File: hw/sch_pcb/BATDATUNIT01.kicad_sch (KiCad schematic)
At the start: 109 parts, among them IC1 MAX14502AETL+, J1 USBC_USB4105-GF-A, J22 HEADER_2x03, J4 46436-9327, J9 SD_Card-FPS009-4200-0, Q1 BC817-25, Q2 BC817-25, Q3 BC817-25, Q4 BC817-25, SW3 KMT031, SW3 SKRTLAE010, SW4 KMT031, SW4 SKRTLAE010, U10 ATMEGA1284P-AU, U10 TCA4307, U11 PCF85263A, U12 TMUX1574DYYR, U2 USBLC6-2SC6, U3 FT260Q-T, U4 PCA9541ABS/01, U6 AT24CS64-SSHM, U6 SHT35-DIS, Y1 8 MHz, Y2 ABS07-120-32.768KHZ-T

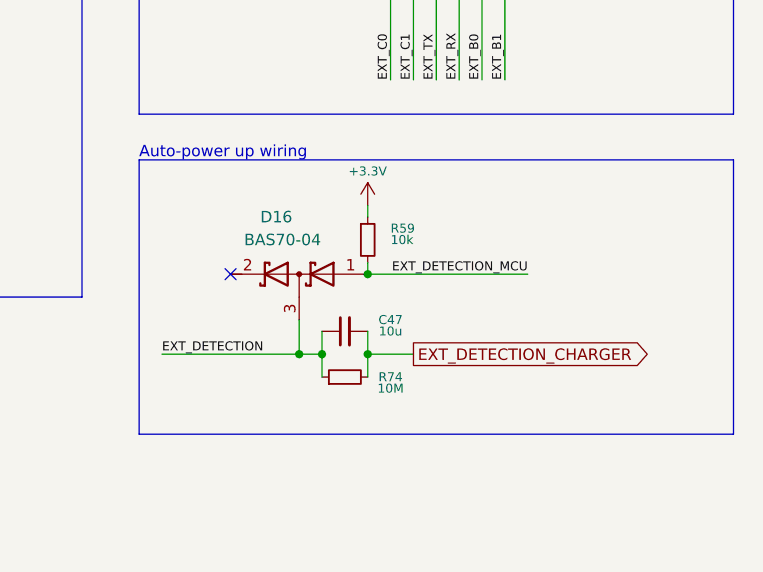
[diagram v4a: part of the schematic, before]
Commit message: Layout update, place and route new added components
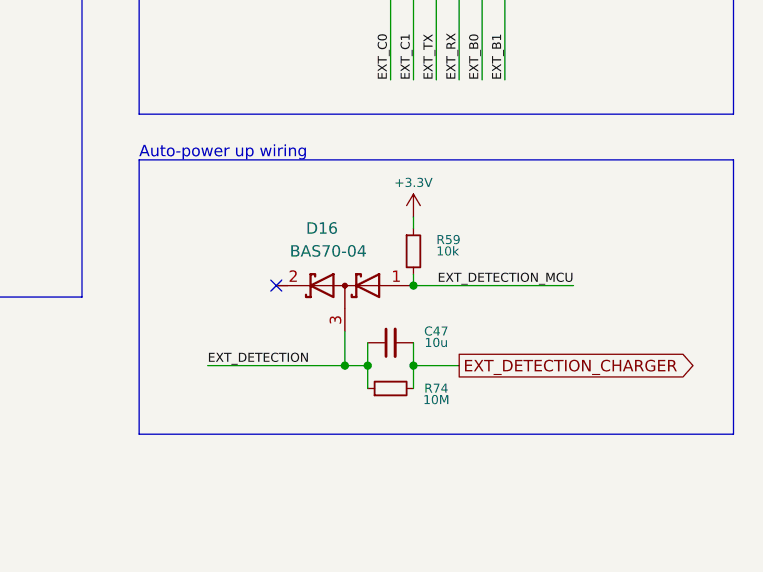
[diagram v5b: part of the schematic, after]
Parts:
- C47: footprint (none) -> Capacitor_SMD:C_0805_2012Metric
- R74: footprint (none) -> Resistor_SMD:R_0805_2012Metric
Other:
- moved on the sheet: C47, D16, R59, R74
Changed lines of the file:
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@@
   (junction (at 80.01 209.55) (diameter 0) (color 0 0 0 0)
   )
-  (junction (at 358.14 241.3) (diameter 0) (color 0 0 0 0)
+  (junction (at 363.22 242.57) (diameter 0) (color 0 0 0 0)
   )
   (junction (at 142.24 248.92) (diameter 0) (color 0 0 0 0)
@@
   (junction (at 40.64 262.89) (diameter 1.016) (color 0 0 0 0)
   )
-  (junction (at 363.22 241.3) (diameter 0) (color 0 0 0 0)
+  (junction (at 368.3 242.57) (diameter 0) (color 0 0 0 0)
   )
   (junction (at 156.21 144.78) (diameter 0) (color 0 0 0 0)
@@
   (junction (at 162.56 35.56) (diameter 0) (color 0 0 0 0)
   )
-  (junction (at 355.6 241.3) (diameter 0) (color 0 0 0 0)
+  (junction (at 360.68 242.57) (diameter 0) (color 0 0 0 0)
   )
   (junction (at 53.34 43.18) (diameter 0) (color 0 0 0 0)
@@
   (junction (at 36.83 262.89) (diameter 1.016) (color 0 0 0 0)
   )
-  (junction (at 363.22 232.41) (diameter 0) (color 0 0 0 0)
+  (junction (at 368.3 233.68) (diameter 0) (color 0 0 0 0)
   )
   (junction (at 275.59 220.98) (diameter 1.016) (color 0 0 0 0)
@@
   (no_connect (at 388.62 173.99))
   (no_connect (at 184.15 182.88))
-  (no_connect (at 347.98 232.41))
+  (no_connect (at 353.06 233.68))
   (no_connect (at 388.62 176.53))
   (no_connect (at 92.71 124.46))
@@
     (stroke (width 0) (type default))
   )
-  (wire (pts (xy 363.22 241.3) (xy 363.22 243.84))
+  (wire (pts (xy 368.3 242.57) (xy 368.3 245.11))
     (stroke (width 0) (type default))
   )
@@
     (stroke (width 0) (type default))
   )
-  (wire (pts (xy 340.36 241.3) (xy 355.6 241.3))
+  (wire (pts (xy 345.44 242.57) (xy 360.68 242.57))
     (stroke (width 0) (type default))
   )
@@
     (stroke (width 0) (type default))
   )
-  (wire (pts (xy 355.6 241.3) (xy 358.14 241.3))
+  (wire (pts (xy 360.68 242.57) (xy 363.22 242.57))
     (stroke (width 0) (type default))
   )
@@
     (stroke (width 0) (type default))
   )
-  (wire (pts (xy 363.22 241.3) (xy 368.3 241.3))
+  (wire (pts (xy 368.3 242.57) (xy 373.38 242.57))
     (stroke (width 0) (type default))
   )
@@
     (stroke (width 0) (type default))
   )
-  (wire (pts (xy 363.22 224.79) (xy 363.22 226.06))
+  (wire (pts (xy 368.3 226.06) (xy 368.3 227.33))
     (stroke (width 0) (type default))
   )
@@
     (stroke (width 0) (type default))
   )
-  (wire (pts (xy 363.22 232.41) (xy 381 232.41))
+  (wire (pts (xy 368.3 233.68) (xy 386.08 233.68))
     (stroke (width 0) (type default))
   )
@@
     (stroke (width 0) (type default))
   )
-  (wire (pts (xy 363.22 231.14) (xy 363.22 232.41))
+  (wire (pts (xy 368.3 232.41) (xy 368.3 233.68))
     (stroke (width 0) (type default))
   )
@@
     (stroke (width 0) (type default))
   )
-  (wire (pts (xy 358.14 238.76) (xy 358.14 241.3))
+  (wire (pts (xy 363.22 240.03) (xy 363.22 242.57))
     (stroke (width 0) (type default))
   )
@@
     (stroke (width 0) (type default))
   )
-  (wire (pts (xy 355.6 237.49) (xy 355.6 241.3))
+  (wire (pts (xy 360.68 238.76) (xy 360.68 242.57))
     (stroke (width 0) (type default))
   )
@@
     (stroke (width 0) (type solid))
   )
-  (wire (pts (xy 358.14 241.3) (xy 358.14 243.84))
+  (wire (pts (xy 363.22 242.57) (xy 363.22 245.11))
     (stroke (width 0) (type default))
   )
@@
     (stroke (width 0) (type default))
   )
-  (wire (pts (xy 363.22 238.76) (xy 363.22 241.3))
+  (wire (pts (xy 368.3 240.03) (xy 368.3 242.57))
     (stroke (width 0) (type default))
   )
@@
     (effects (font (size 1 1)) (justify right bottom))
   )
-  (label "EXT_DETECTION" (at 340.36 241.3 0) (fields_autoplaced)
+  (label "EXT_DETECTION" (at 345.44 242.57 0) (fields_autoplaced)
     (effects (font (size 1 1)) (justify left bottom))
   )
@@
     (effects (font (size 1 1)) (justify left bottom))
   )
-  (label "EXT_DETECTION_MCU" (at 381 232.41 180) (fields_autoplaced)
+  (label "EXT_DETECTION_MCU" (at 386.08 233.68 180) (fields_autoplaced)
     (effects (font (size 1 1)) (justify right bottom))
   )
@@
     )
   )
-  (global_label "EXT_DETECTION_CHARGER" (shape output) (at 368.3 241.3 0) (fields_autoplaced)
+  (global_label "EXT_DETECTION_CHARGER" (shape output) (at 373.38 242.57 0) (fields_autoplaced)
     (effects (font (size 1.27 1.27)) (justify left))
-    (property "Intersheetrefs" "${INTERSHEET_REFS}" (at 395.2336 241.3 0)
+    (property "Intersheetrefs" "${INTERSHEET_REFS}" (at 400.3136 242.57 0)
       (effects (font (size 1.27 1.27)) (justify left) hide)
     )
@@
     )
   )
-  (symbol (lib_id "Device:R_Small") (at 363.22 228.6 0) (unit 1)
+  (symbol (lib_id "Device:R_Small") (at 368.3 229.87 0) (unit 1)
     (in_bom yes) (on_board yes) (dnp no)
-    (property "Reference" "R59" (at 365.76 227.33 0)
+    (property "Reference" "R59" (at 370.84 228.6 0)
       (effects (font (size 1 1)) (justify left))
     )
-    (property "Value" "10k" (at 365.76 228.6 0)
+    (property "Value" "10k" (at 370.84 229.87 0)
       (effects (font (size 1 1)) (justify left))
     )
-    (property "Footprint" "Resistor_SMD:R_0805_2012Metric" (at 363.22 228.6 0)
+    (property "Footprint" "Resistor_SMD:R_0805_2012Metric" (at 368.3 229.87 0)
       (effects (font (size 1 1)) hide)
     )
-    (property "Datasheet" "~" (at 363.22 228.6 0)
+    (property "Datasheet" "~" (at 368.3 229.87 0)
       (effects (font (size 1 1)) hide)
     )
-    (property "UST_ID" "5c70984612875079b91f899f" (at 363.22 228.6 0)
+    (property "UST_ID" "5c70984612875079b91f899f" (at 368.3 229.87 0)
       (effects (font (size 1 1)) hide)
     )
@@
     )
   )
-  (symbol (lib_id "Device:C_Small") (at 360.68 238.76 90) (unit 1)
+  (symbol (lib_id "Device:C_Small") (at 365.76 240.03 90) (unit 1)
     (in_bom yes) (on_board yes) (dnp no)
-    (property "Reference" "C47" (at 365.76 237.49 90)
+    (property "Reference" "C47" (at 370.84 238.76 90)
       (effects (font (size 1 1)))
     )
-    (property "Value" "10u" (at 365.76 238.76 90)
+    (property "Value" "10u" (at 370.84 240.03 90)
       (effects (font (size 1 1)))
     )
-    (property "Footprint" "" (at 360.68 238.76 0)
+    (property "Footprint" "Capacitor_SMD:C_0805_2012Metric" (at 365.76 240.03 0)
       (effects (font (size 1.27 1.27)) hide)
     )
-    (property "Datasheet" "~" (at 360.68 238.76 0)
+    (property "Datasheet" "~" (at 365.76 240.03 0)
       (effects (font (size 1.27 1.27)) hide)
     )
@@
     )
   )
-  (symbol (lib_id "power:+3.3V") (at 363.22 224.79 0) (unit 1)
+  (symbol (lib_id "power:+3.3V") (at 368.3 226.06 0) (unit 1)
     (in_bom yes) (on_board yes) (dnp no)
-    (property "Reference" "#PWR0110" (at 363.22 228.6 0)
+    (property "Reference" "#PWR0110" (at 368.3 229.87 0)
       (effects (font (size 1 1)) hide)
     )
-    (property "Value" "+3.3V" (at 363.22 220.98 0)
+    (property "Value" "+3.3V" (at 368.3 222.25 0)
       (effects (font (size 1 1)))
     )
-    (property "Footprint" "" (at 363.22 224.79 0)
+    (property "Footprint" "" (at 368.3 226.06 0)
       (effects (font (size 1 1)) hide)
     )
-    (property "Datasheet" "" (at 363.22 224.79 0)
+    (property "Datasheet" "" (at 368.3 226.06 0)
       (effects (font (size 1 1)) hide)
     )
@@
     )
   )
-  (symbol (lib_id "Device:D_Schottky_Dual_Series_AKC") (at 355.6 232.41 0) (mirror y) (unit 1)
+  (symbol (lib_id "Device:D_Schottky_Dual_Series_AKC") (at 360.68 233.68 0) (mirror y) (unit 1)
     (in_bom yes) (on_board yes) (dnp no)
-    (property "Reference" "D16" (at 353.06 226.06 0)
+    (property "Reference" "D16" (at 358.14 227.33 0)
       (effects (font (size 1.27 1.27)))
     )
-    (property "Value" "BAS70-04" (at 353.7585 228.6 0)
+    (property "Value" "BAS70-04" (at 358.8385 229.87 0)
       (effects (font (size 1.27 1.27)))
     )
-    (property "Footprint" "Package_TO_SOT_SMD:SOT-23" (at 355.6 232.41 0)
+    (property "Footprint" "Package_TO_SOT_SMD:SOT-23" (at 360.68 233.68 0)
       (effects (font (size 1.27 1.27)) hide)
     )
-    (property "Datasheet" "~" (at 355.6 232.41 0)
+    (property "Datasheet" "~" (at 360.68 233.68 0)
       (effects (font (size 1.27 1.27)) hide)
     )
@@
     )
   )
-  (symbol (lib_id "Device:R_Small") (at 360.68 243.84 90) (unit 1)
+  (symbol (lib_id "Device:R_Small") (at 365.76 245.11 90) (unit 1)
     (in_bom yes) (on_board yes) (dnp no)
-    (property "Reference" "R74" (at 365.76 243.84 90)
+    (property "Reference" "R74" (at 370.84 245.11 90)
       (effects (font (size 1 1)))
     )
-    (property "Value" "10M" (at 365.76 245.11 90)
+    (property "Value" "10M" (at 370.84 246.38 90)
       (effects (font (size 1 1)))
     )
-    (property "Footprint" "" (at 360.68 243.84 0)
+    (property "Footprint" "Resistor_SMD:R_0805_2012Metric" (at 365.76 245.11 0)
       (effects (font (size 1.27 1.27)) hide)
     )
-    (property "Datasheet" "~" (at 360.68 243.84 0)
+    (property "Datasheet" "~" (at 365.76 245.11 0)
       (effects (font (size 1.27 1.27)) hide)
     )

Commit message: solve drc, fill ust_id
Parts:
- D16: UST_ID (none) -> 5c70984512875079b91f88b6
- JP8: UST_ID (none) -> x
- R74: UST_ID (none) -> 5c70984712875079b91f8aae
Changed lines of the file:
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@@
+      (effects (font (size 1.27 1.27)) hide)
+    )
+    (property "UST_ID" "5c70984512875079b91f88b6" (at 360.68 233.68 0)
       (effects (font (size 1.27 1.27)) hide)
     )
@@
       (effects (font (size 1.27 1.27)) hide)
     )
+    (property "UST_ID" "x" (at 358.14 77.47 0)
+      (effects (font (size 1.27 1.27)) hide)
+    )
     (pin "1")
     (pin "2")
@@
       (effects (font (size 1.27 1.27)) hide)
     )
+    (property "UST_ID" "5c70984712875079b91f8aae" (at 365.76 245.11 0)
+      (effects (font (size 1.27 1.27)) hide)
+    )
